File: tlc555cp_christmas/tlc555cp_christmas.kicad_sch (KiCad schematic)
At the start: 18 parts, among them SW1 SW_MEC_5E, U1 TLC555xP

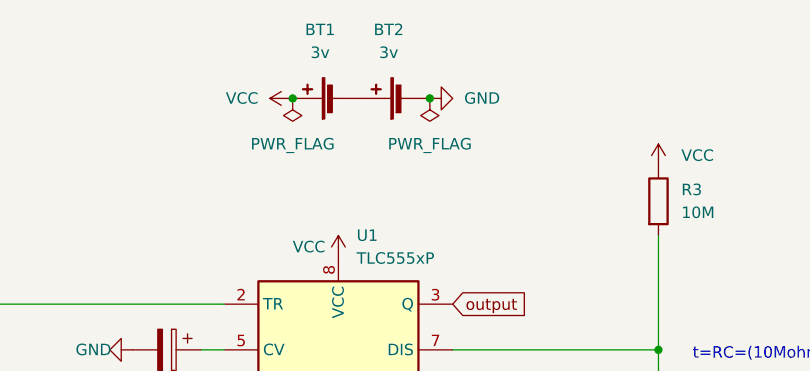
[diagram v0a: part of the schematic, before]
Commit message: Fix switch footprint pad assignment.
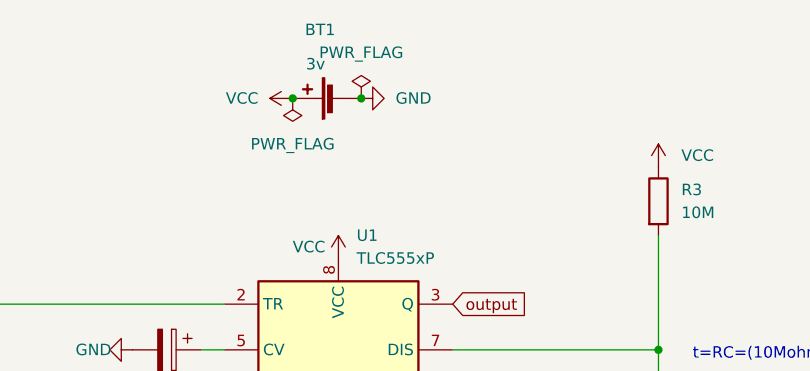
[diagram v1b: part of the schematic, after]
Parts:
- removed BT2: 3v, footprints:1066, symbol Device:Battery_Cell
- SW1: footprint Button_Switch_THT:SW_PUSH-12mm -> footprints:SW_PUSH-12mm_kody
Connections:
- net GND: now also BT1.2 (-)
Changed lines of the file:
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@@
   (junction (at 147.32 55.88) (diameter 0) (color 0 0 0 0)
   )
-  (junction (at 162.56 55.88) (diameter 0) (color 0 0 0 0)
-  )
   (junction (at 100.33 81.28) (diameter 0) (color 0 0 0 0)
   )
@@
   )
   (junction (at 187.96 83.82) (diameter 0) (color 0 0 0 0)
+  )
+  (junction (at 154.94 55.88) (diameter 0) (color 0 0 0 0)
   )
   (junction (at 97.79 91.44) (diameter 0) (color 0 0 0 0)
@@
     (pin "2")
   )
-  (symbol (lib_id "power:PWR_FLAG") (at 162.56 55.88 180) (unit 1)
-    (in_bom yes) (on_board yes) (fields_autoplaced)
-    (property "Reference" "#FLG0101" (id 0) (at 162.56 57.785 0)
-      (effects (font (size 1.27 1.27)) hide)
-    )
-    (property "Value" "PWR_FLAG" (id 1) (at 162.56 60.96 0))
-    (property "Footprint" "" (id 2) (at 162.56 55.88 0)
-      (effects (font (size 1.27 1.27)) hide)
-    )
-    (property "Datasheet" "~" (id 3) (at 162.56 55.88 0)
+  (symbol (lib_id "power:PWR_FLAG") (at 154.94 55.88 0) (unit 1)
+    (in_bom yes) (on_board yes) (fields_autoplaced)
+    (property "Reference" "#FLG0101" (id 0) (at 154.94 53.975 0)
+      (effects (font (size 1.27 1.27)) hide)
+    )
+    (property "Value" "PWR_FLAG" (id 1) (at 154.94 50.8 0))
+    (property "Footprint" "" (id 2) (at 154.94 55.88 0)
+      (effects (font (size 1.27 1.27)) hide)
+    )
+    (property "Datasheet" "~" (id 3) (at 154.94 55.88 0)
       (effects (font (size 1.27 1.27)) hide)
     )
@@
     (pin "1")
   )
-  (symbol (lib_id "power:GND") (at 162.56 55.88 90) (unit 1)
-    (in_bom yes) (on_board yes) (fields_autoplaced)
-    (property "Reference" "#PWR0113" (id 0) (at 168.91 55.88 0)
-      (effects (font (size 1.27 1.27)) hide)
-    )
-    (property "Value" "GND" (id 1) (at 166.37 55.8799 90)
+  (symbol (lib_id "power:GND") (at 154.94 55.88 90) (unit 1)
+    (in_bom yes) (on_board yes) (fields_autoplaced)
+    (property "Reference" "#PWR0113" (id 0) (at 161.29 55.88 0)
+      (effects (font (size 1.27 1.27)) hide)
+    )
+    (property "Value" "GND" (id 1) (at 158.75 55.8799 90)
       (effects (font (size 1.27 1.27)) (justify right))
     )
-    (property "Footprint" "" (id 2) (at 162.56 55.88 0)
-      (effects (font (size 1.27 1.27)) hide)
-    )
-    (property "Datasheet" "" (id 3) (at 162.56 55.88 0)
+    (property "Footprint" "" (id 2) (at 154.94 55.88 0)
+      (effects (font (size 1.27 1.27)) hide)
+    )
+    (property "Datasheet" "" (id 3) (at 154.94 55.88 0)
       (effects (font (size 1.27 1.27)) hide)
     )
@@
   )
   (symbol (lib_id "Device:Battery_Cell") (at 152.4 55.88 90) (unit 1)
-    (in_bom yes) (on_board yes) (fields_autoplaced)
+    (in_bom yes) (on_board yes)
     (property "Reference" "BT1" (id 0) (at 150.368 48.26 90))
-    (property "Value" "3v" (id 1) (at 150.368 50.8 90))
+    (property "Value" "3v" (id 1) (at 149.86 52.07 90))
     (property "Footprint" "footprints:1066" (id 2) (at 150.876 55.88 90)
       (effects (font (size 1.27 1.27)) hide)
@@
       (effects (font (size 1.27 1.27)) (justify left))
     )
-    (property "Footprint" "Button_Switch_THT:SW_PUSH-12mm" (id 2) (at 105.41 86.36 0)
+    (property "Footprint" "footprints:SW_PUSH-12mm_kody" (id 2) (at 105.41 86.36 0)
       (effects (font (size 1.27 1.27)) hide)
     )
@@
     (pin "1")
   )
-  (symbol (lib_id "Device:Battery_Cell") (at 160.02 55.88 90) (unit 1)
-    (in_bom yes) (on_board yes) (fields_autoplaced)
-    (property "Reference" "BT2" (id 0) (at 157.988 48.26 90))
-    (property "Value" "3v" (id 1) (at 157.988 50.8 90))
-    (property "Footprint" "footprints:1066" (id 2) (at 158.496 55.88 90)
-      (effects (font (size 1.27 1.27)) hide)
-    )
-    (property "Datasheet" "~" (id 3) (at 158.496 55.88 90)
-      (effects (font (size 1.27 1.27)) hide)
-    )
-    (pin "1")
-    (pin "2")
-  )
   (symbol (lib_id "Device:LED") (at 118.11 118.11 180) (unit 1)
     (in_bom yes) (on_board yes) (fields_autoplaced)
@@
       (reference "BT1") (unit 1) (value "3v") (footprint "footprints:1066")
     )
-    (path "/baf3ad47-9fcb-47b8-a30d-b217ef6ea7cb"
-      (reference "BT2") (unit 1) (value "3v") (footprint "footprints:1066")
-    )
     (path "/3821a767-0e81-4328-a97c-d76bf643cb33"
       (reference "C1") (unit 1) (value "0.1u") (footprint "Capacitor_THT:CP_Radial_D4.0mm_P2.00mm")
@@
     )
     (path "/6e6b62e5-8a91-4770-862a-fd16eaf92d42"
-      (reference "SW1") (unit 1) (value "SW_MEC_5E") (footprint "Button_Switch_THT:SW_PUSH-12mm")
+      (reference "SW1") (unit 1) (value "SW_MEC_5E") (footprint "footprints:SW_PUSH-12mm_kody")
     )
     (path "/34e93660-1191-41a2-97f5-a003afb368ac"
